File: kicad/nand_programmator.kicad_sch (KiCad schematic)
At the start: 42 parts, among them J1 Conn_01x04, J2 Conn_01x03, J3 Conn_02x12_Odd_Even_Left, J4 Conn_02x12_Odd_Even_Right, J5 BOOT0, J6 ~{RST}, P1 USB_C_Receptacle_USB2.0_16P, U1 AMS1117-3.3, U2 STM32F103VCT6, Y1 8MHz 18pF

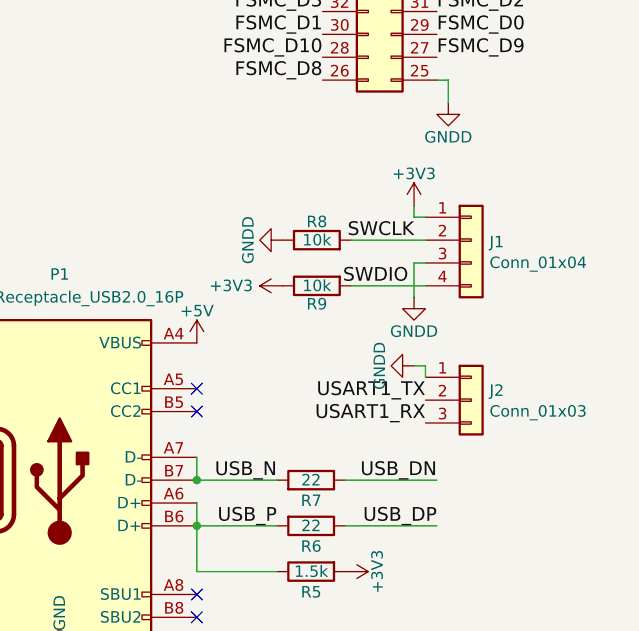
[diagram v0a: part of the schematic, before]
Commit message: Add LCSC part number metadata through kicad-jlcpcb-tools
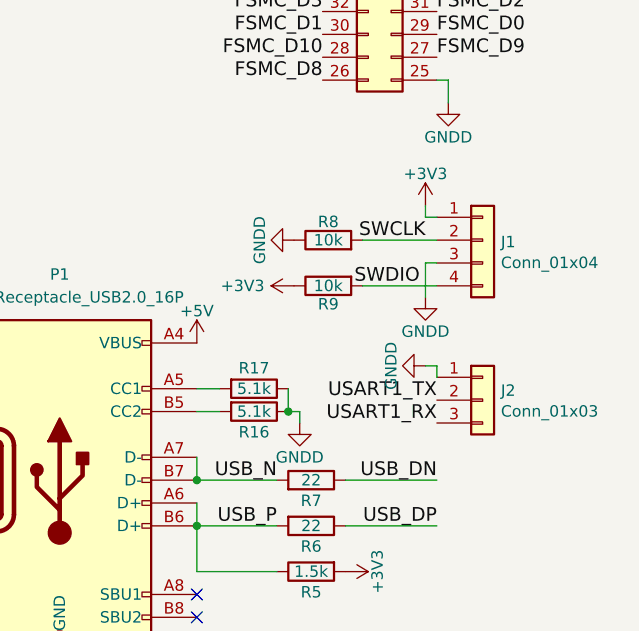
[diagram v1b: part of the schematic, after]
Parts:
- added R16, R17: 5.1k, lib_fp:R_0805_2012Metric_Pad1.15x1.40mm_HandSolder, symbol Device:R
- P1: footprint Connector_USB:USB_C_Receptacle_HCTL_HC-TYPE-C-16P-01A -> Connector_USB:USB_C_Receptacle_GCT_USB4105-xx-A_16P_TopMnt_Horizontal
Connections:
- net GNDD: now also R16.1, R17.1
- net at P1.A5 (CC1): now also R17.2
- net at P1.B5 (CC2): now also R16.2
- no-connect marks 64 -> 62
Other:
- moved on the sheet: J1, J2, R8, R9
